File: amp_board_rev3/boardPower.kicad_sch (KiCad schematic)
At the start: 4 parts, among them J1 CT3151V1-0, J2 CT3151V1-2

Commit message: all routed
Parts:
- added J4: CT3151V1-0, 726_footprints:banana_plug_CT3151V1-0, symbol _PHASE:CT3151V1-0
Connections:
- net GND: now also J4.1, J4.2, J4.3, J4.4; no longer C1.2, C2.2 (-), J1.1, J1.2, J1.3, J1.4
- new net VSS: C1.2, C2.2 (-), J1.1, J1.2, J1.3, J1.4
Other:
- moved on the sheet: J1

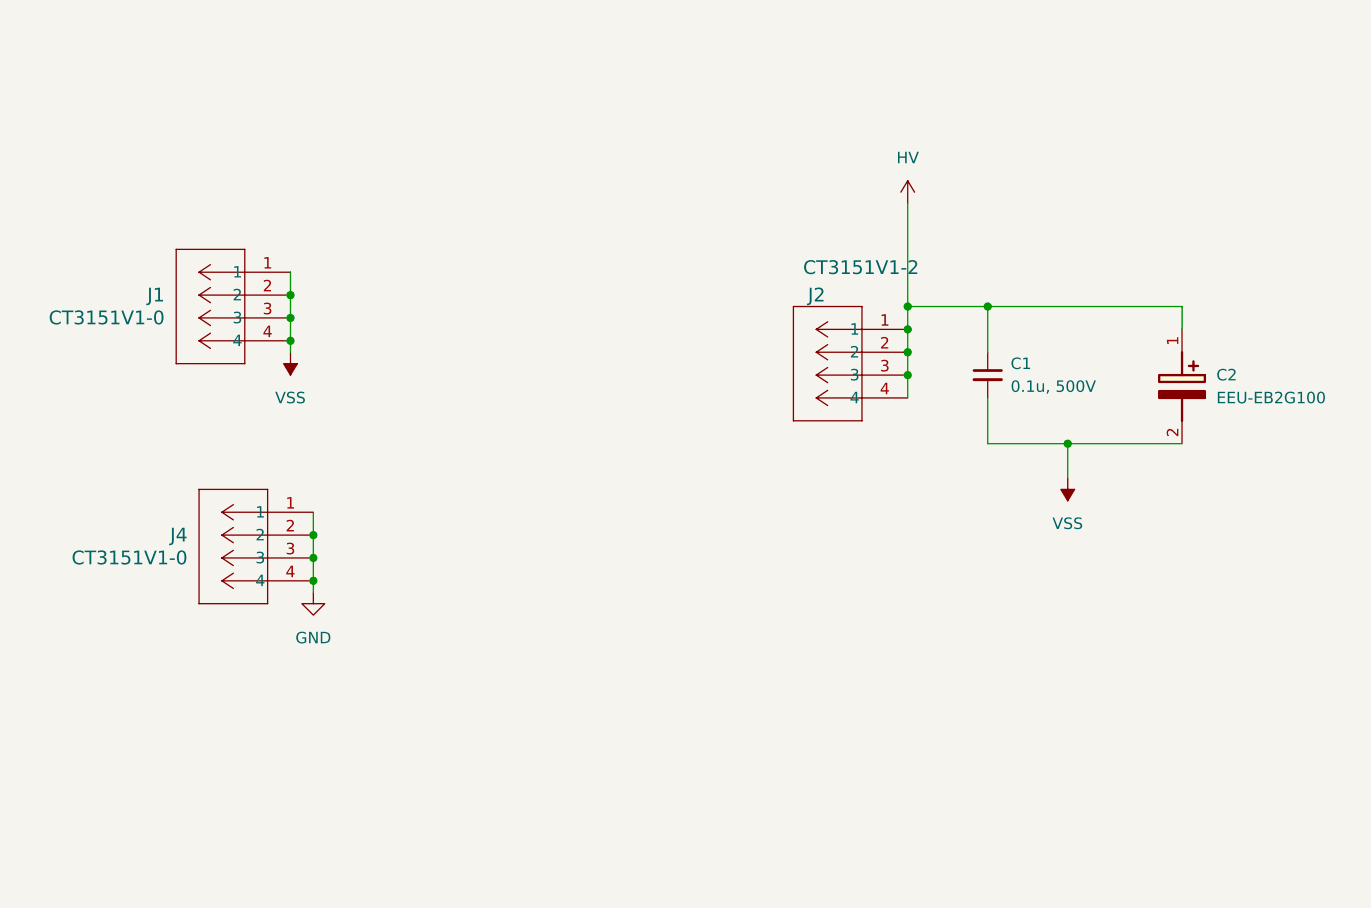
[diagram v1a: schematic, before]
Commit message: updated ground references in schematic
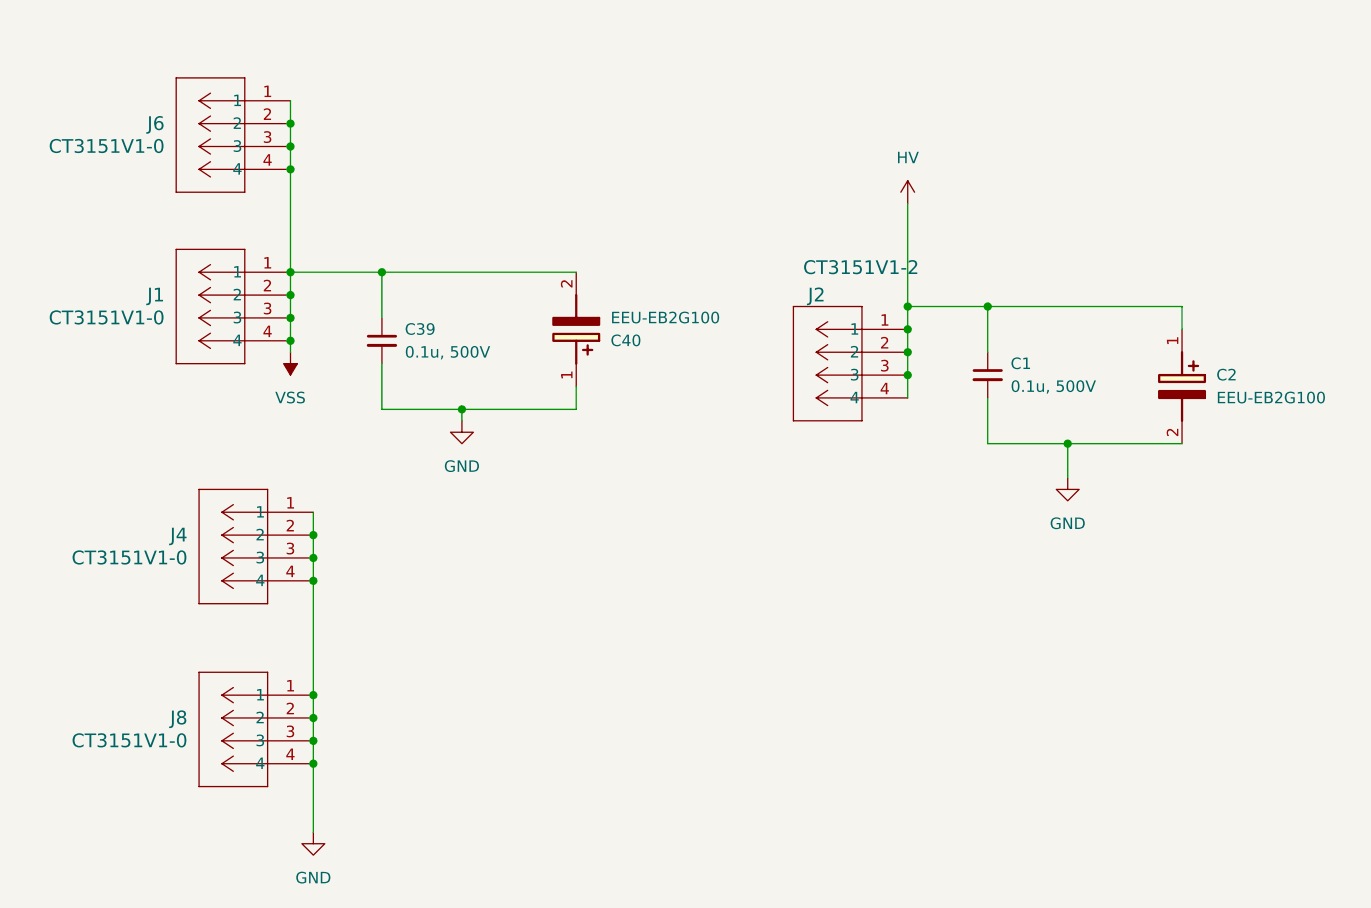
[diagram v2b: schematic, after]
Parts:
- added C39: 0.1u, 500V, Capacitor_SMD:C_1812_4532Metric, symbol Device:C_Small
- added C40: EEU-EB2G100, 726_footprints:EEU-EB2G100, symbol _PHASE:EEU-EB2G100
- added J6, J8: CT3151V1-0, 726_footprints:banana_plug_CT3151V1-0, symbol _PHASE:CT3151V1-0
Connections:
- net GND: now also C1.2, C2.2 (-), C39.2, C40.1 (+), J8.1, J8.2, J8.3, J8.4
- net VSS: now also C39.1, C40.2 (-), J6.1, J6.2, J6.3, J6.4; no longer C1.2, C2.2 (-)

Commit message: updates based on 11/14 meeting
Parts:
- C1, C39: footprint Capacitor_SMD:C_1812_4532Metric -> (none)
- C2, C40: footprint 726_footprints:EEU-EB2G100 -> CAPPRD500W65D1000H2200
- J1, J2, J4, J6, J8: footprint 726_footprints:banana_plug_CT3151V1-0 -> 0_726_footprints:banana_plug_CT3151V1-0
